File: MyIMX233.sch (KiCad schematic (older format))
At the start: 91 parts, among them IC1 iMX233, IC2 DDR_SDRAM_MT46_x16, J1 USB_OTG, P1 4p2, P2 1v2, P3 VDDA1v8, P4 2v5, P5 3v3, P6 1v, SW1 SWITCH_PUSHBUTTON, Y1 24Mhz

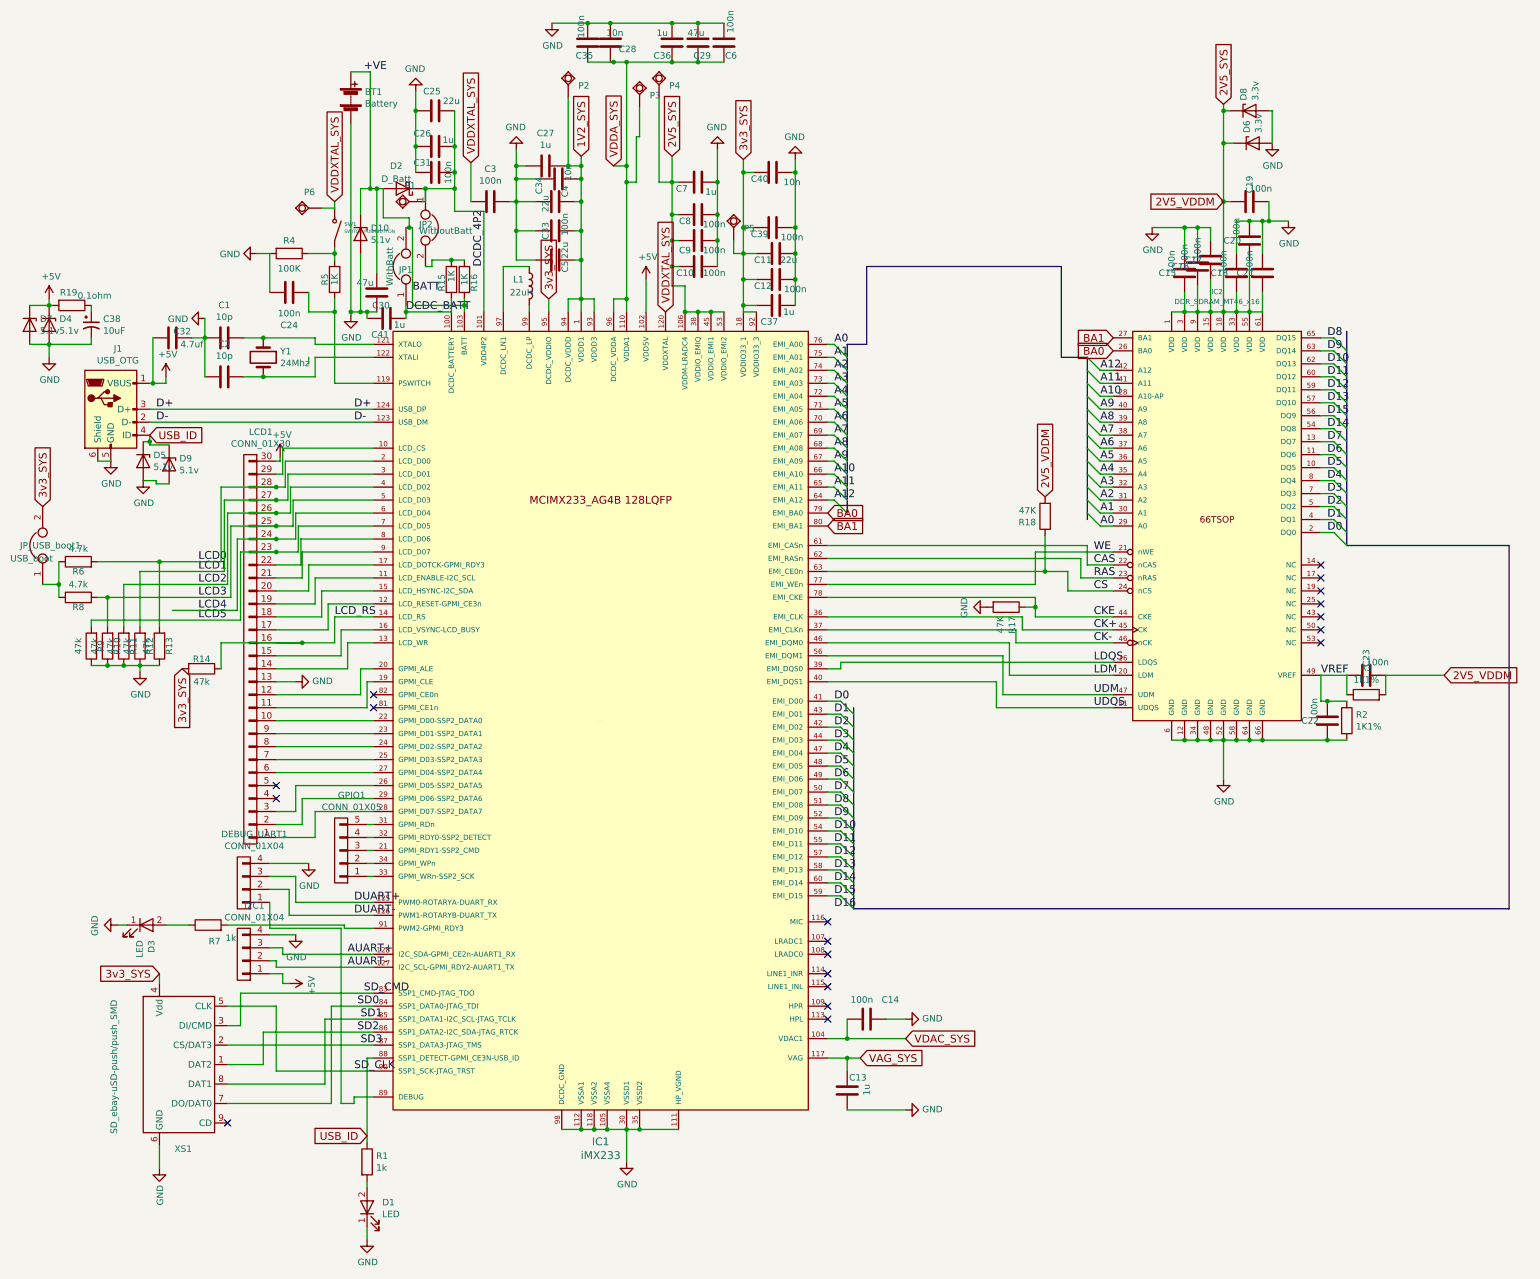
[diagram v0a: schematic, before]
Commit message: added  SD data resistors, clk nCLK resistor, series resistor to stop oscillation
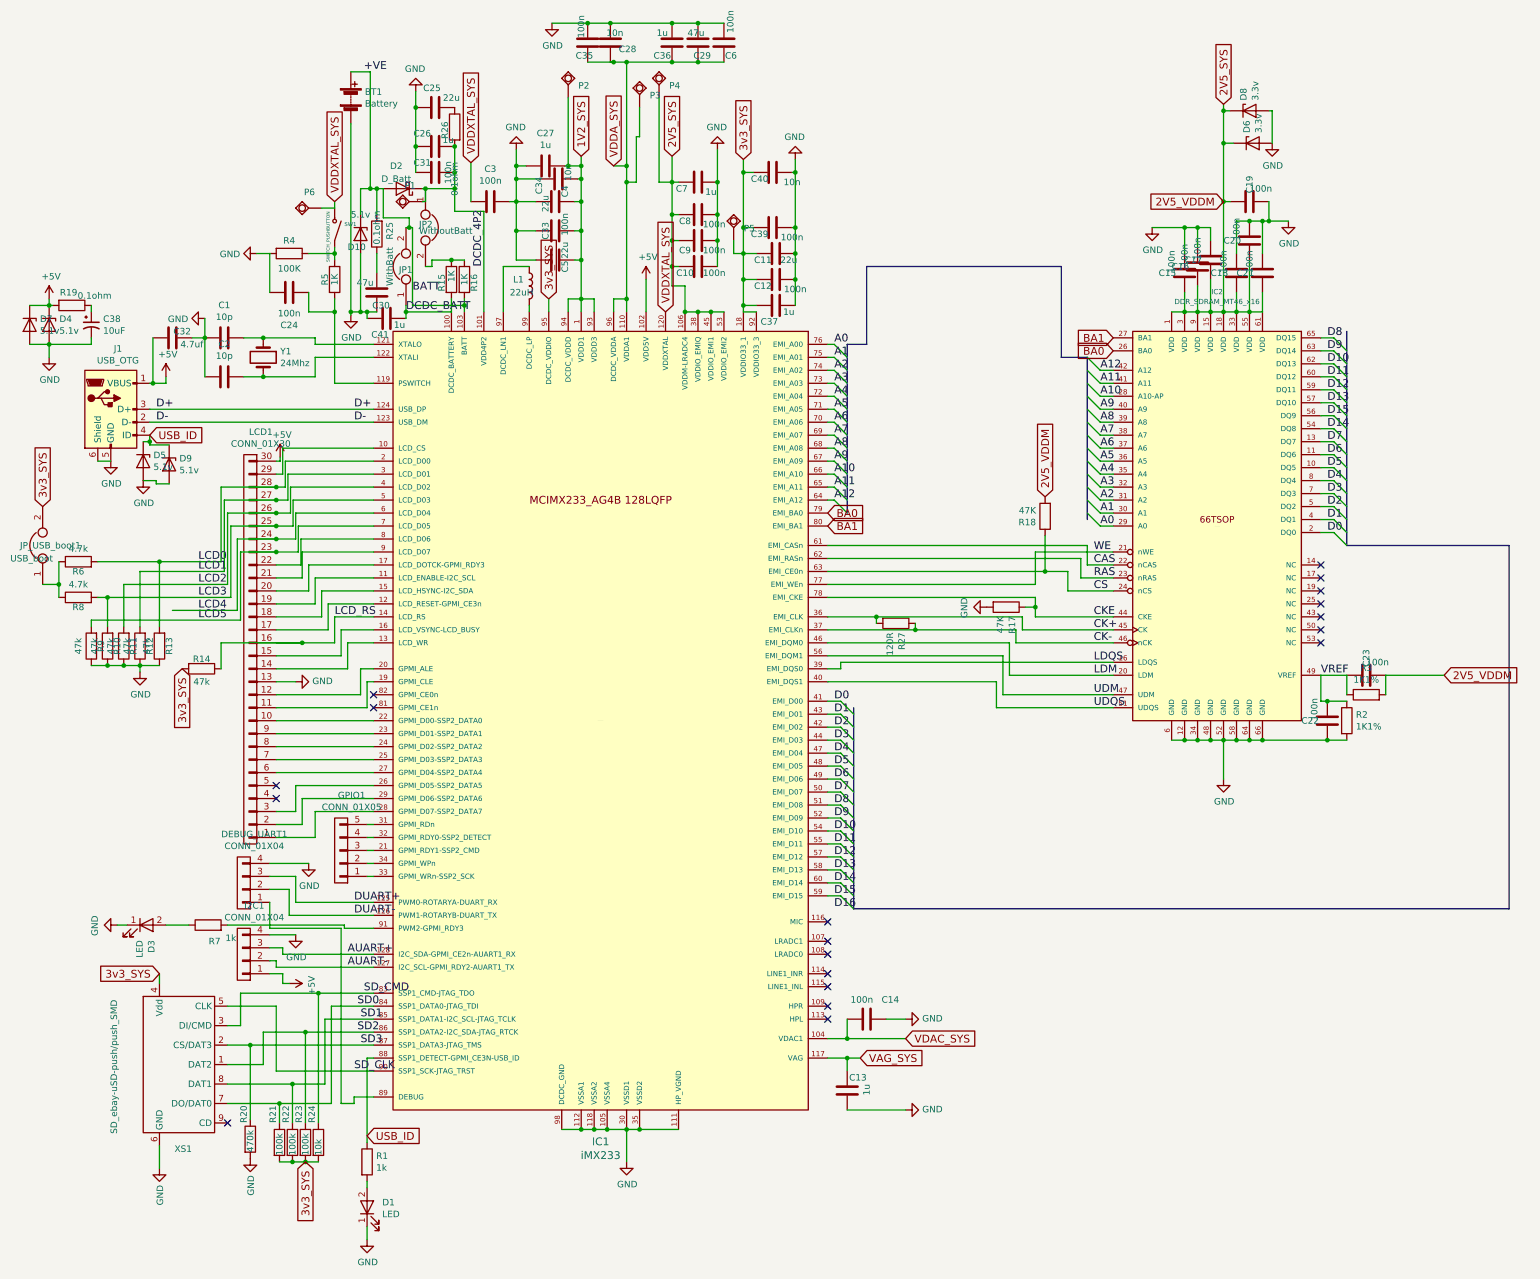
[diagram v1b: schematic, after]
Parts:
- added R20: 470k, Resistors_SMD:R_0603_HandSoldering, symbol R
- added R21, R22, R23: 100k, Resistors_SMD:R_0603_HandSoldering, symbol R
- added R24: 10k, Resistors_SMD:R_0603_HandSoldering, symbol R
- added R25, R26: 0.1ohm, Resistors_SMD:R_0603_HandSoldering, symbol R
- added R27: 120R, Resistors_SMD:R_0603, symbol R
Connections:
- net +VE: now also R25.2; no longer C30.1
- net 3v3_SYS: now also R21.2, R22.2, R23.2, R24.2
- net CK+: now also R27.2
- net CK-: now also R27.1
- net DCDC_4P2: now also R26.2; no longer C25.2
- net GND: now also R20.2
- net SD0: now also R21.1
- net SD1: now also R22.1
- net SD2: now also R23.1
- net SD3: now also R20.1
- net SD_CMD: now also R24.1
- new net: C25.2, R26.1
- new net: C30.1, R25.1
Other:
- moved on the sheet: C25
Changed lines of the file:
@@
 P 2950 2100
 F 0 "SW1" V 2924 2175 30  0000 L CNN
-F 1 "SWITCH_PUSHBUTTON" V 2980 2175 25  0000 L CNN
+F 1 "SWITCH_PUSHBUTTON" H 2825 2050 25  0000 L CNN
 F 2 "Buttons_Switches_THT:SW_PUSH_6mm" H 2950 2100 60  0001 C CNN
 F 3 "" H 2950 2100 60  0001 C CNN
@@
 L C C25
 U 1 1 592FCC84
-P 3725 1200
-F 0 "C25" V 3875 1225 50  0000 C CNN
-F 1 "22u" V 3800 1075 50  0000 C CNN
-F 2 "Capacitors_SMD:C_0805_HandSoldering" H 3763 1050 50  0001 C CNN
-F 3 "" H 3725 1200 50  0001 C CNN
-	1    3725 1200
+P 3725 1175
+F 0 "C25" V 3875 1200 50  0000 C CNN
+F 1 "22u" V 3800 1050 50  0000 C CNN
+F 2 "Capacitors_SMD:C_0805_HandSoldering" H 3763 1025 50  0001 C CNN
+F 3 "" H 3725 1175 50  0001 C CNN
+	1    3725 1175
 	0    -1   -1   0
 $EndComp
@@
 	1    0    0    -1
 $EndComp
-Text GLabel 3200 9100 0    60   Input ~ 0
+Text GLabel 3200 9100 2    60   Input ~ 0
 USB_ID
 Text GLabel 1525 3700 2    60   Input ~ 0
@@
 	2250 2950 2800 2950
 Connection ~ 2400 2950
-Wire Wire Line
-	2750 3100 2750 3150
 Wire Wire Line
 	1950 2800 1950 3250
@@
 Wire Wire Line
 	3575 1050 3575 1675
-Connection ~ 3575 1200
-Wire Wire Line
-	3875 1975 3875 1200
 Connection ~ 3875 1675
 Connection ~ 3875 1475
 Connection ~ 3575 1475
 Wire Wire Line
-	3625 1800 3875 1800
+	3875 1800 3625 1800
 Connection ~ 3875 1800
 Wire Wire Line
@@
 Connection ~ 3525 2100
 Wire Wire Line
-	3275 1800 3275 2450
-Wire Wire Line
 	3275 2750 3075 2750
 Connection ~ 3075 2750
@@
 U 1 1 59A40581
 P 3150 2150
-F 0 "D10" V 3104 2229 50  0000 L CNN
-F 1 "5.1v" V 3195 2229 50  0000 L CNN
+F 0 "D10" V 3250 2050 50  0000 L CNN
+F 1 "5.1v" V 3000 2075 50  0000 L CNN
 F 2 "Diodes_SMD:D_SOD-323_HandSoldering" H 3150 2150 50  0001 C CNN
 F 3 "" H 3150 2150 50  0001 C CNN
@@
 	3150 2300 3150 2750
 Connection ~ 3150 2750
+$Comp
+L R R26
+U 1 1 59A340AA
+P 3875 1325
+F 0 "R26" V 3950 1300 50  0000 C CNN
+F 1 "0.1ohm" V 3875 925 50  0000 C CNN
+F 2 "Resistors_SMD:R_0603_HandSoldering" V 3805 1325 50  0001 C CNN
+F 3 "" H 3875 1325 50  0001 C CNN
+	1    3875 1325
+	-1   0    0    -1
+$EndComp
+Connection ~ 3575 1175
+$Comp
+L R R25
+U 1 1 59A38C82
+P 3275 2150
+F 0 "R25" V 3175 2125 50  0000 C CNN
+F 1 "0.1ohm" V 3275 2100 50  0000 C CNN
+F 2 "Resistors_SMD:R_0603_HandSoldering" V 3205 2150 50  0001 C CNN
+F 3 "" H 3275 2150 50  0001 C CNN
+	1    3275 2150
+	-1   0    0    1
+$EndComp
+Wire Wire Line
+	3275 2300 3275 2450
+Wire Wire Line
+	3275 2000 3275 1800
+$Comp
+L R R20
+U 1 1 59A41AE4
+P 2300 9125
+F 0 "R20" V 2250 9250 50  0000 L CNN
+F 1 "470k" V 2300 9025 50  0000 L CNN
+F 2 "Resistors_SMD:R_0603_HandSoldering" V 2230 9125 50  0001 C CNN
+F 3 "" H 2300 9125 50  0001 C CNN
+	1    2300 9125
+	1    0    0    -1
+$EndComp
+$Comp
+L GND #PWR032
+U 1 1 59A429AF
+P 2300 9275
+F 0 "#PWR032" H 2300 9025 50  0001 C CNN
+F 1 "GND" V 2305 9147 50  0000 R CNN
+F 2 "" H 2300 9275 50  0001 C CNN
+F 3 "" H 2300 9275 50  0001 C CNN
+	1    2300 9275
+	1    0    0    -1
+$EndComp
+Wire Wire Line
+	2300 8975 2300 8400
+Connection ~ 2300 8400
+$Comp
+L R R27
+U 1 1 59A44B82
+P 7275 5150
+F 0 "R27" H 7345 5196 50  0000 L CNN
+F 1 "120R" H 7345 5105 50  0000 L CNN
+F 2 "Resistors_SMD:R_0603" V 7205 5150 50  0001 C CNN
+F 3 "" H 7275 5150 50  0001 C CNN
+	1    7275 5150
+	0    1    1    0
+$EndComp
+Wire Wire Line
+	7125 5150 7125 5100
+Connection ~ 7125 5100
+Wire Wire Line
+	7425 5150 7425 5200
+Connection ~ 7425 5200
+$Comp
+L R R21
+U 1 1 59A4733A
+P 2525 9150
+F 0 "R21" V 2475 9300 50  0000 L CNN
+F 1 "100k" V 2525 9050 50  0000 L CNN
+F 2 "Resistors_SMD:R_0603_HandSoldering" V 2455 9150 50  0001 C CNN
+F 3 "" H 2525 9150 50  0001 C CNN
+	1    2525 9150
+	1    0    0    -1
+$EndComp
+Wire Wire Line
+	2825 9000 2825 8000
+Connection ~ 2825 8000
+Wire Wire Line
+	2725 9000 2725 8300
+Connection ~ 2725 8300
+Wire Wire Line
+	2525 9300 2825 9300
+Connection ~ 2725 9300
+Connection ~ 2625 9300
+Text GLabel 2725 9300 3    60   Input ~ 0
+3v3_SYS
+$Comp
+L R R22
+U 1 1 59A4BB47
+P 2625 9150
+F 0 "R22" V 2575 9300 50  0000 L CNN
+F 1 "100k" V 2625 9050 50  0000 L CNN
+F 2 "Resistors_SMD:R_0603_HandSoldering" V 2555 9150 50  0001 C CNN
+F 3 "" H 2625 9150 50  0001 C CNN
+	1    2625 9150
+	1    0    0    -1
+$EndComp
+$Comp
+L R R23
+U 1 1 59A4BC29
+P 2725 9150
+F 0 "R23" V 2675 9300 50  0000 L CNN
+F 1 "100k" V 2725 9050 50  0000 L CNN
+F 2 "Resistors_SMD:R_0603_HandSoldering" V 2655 9150 50  0001 C CNN
+F 3 "" H 2725 9150 50  0001 C CNN
+	1    2725 9150
+	1    0    0    -1
+$EndComp
+$Comp
+L R R24
+U 1 1 59A4BD01
+P 2825 9150
+F 0 "R24" V 2775 9300 50  0000 L CNN
+F 1 "10k" V 2825 9050 50  0000 L CNN
+F 2 "Resistors_SMD:R_0603_HandSoldering" V 2755 9150 50  0001 C CNN
+F 3 "" H 2825 9150 50  0001 C CNN
+	1    2825 9150
+	1    0    0    -1
+$EndComp
+Wire Wire Line
+	3875 1975 3875 1475
+Wire Wire Line
+	2625 9000 2625 8700
+Connection ~ 2625 8700
+Wire Wire Line
+	2525 9000 2525 8850
+Connection ~ 2525 8850
 $EndSCHEMATC

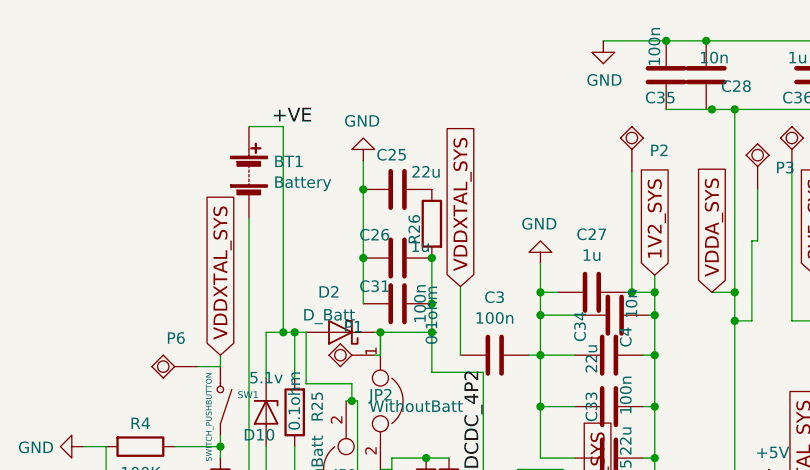
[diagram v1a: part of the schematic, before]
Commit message: added optional 22uf electrolyte cap in 4p2
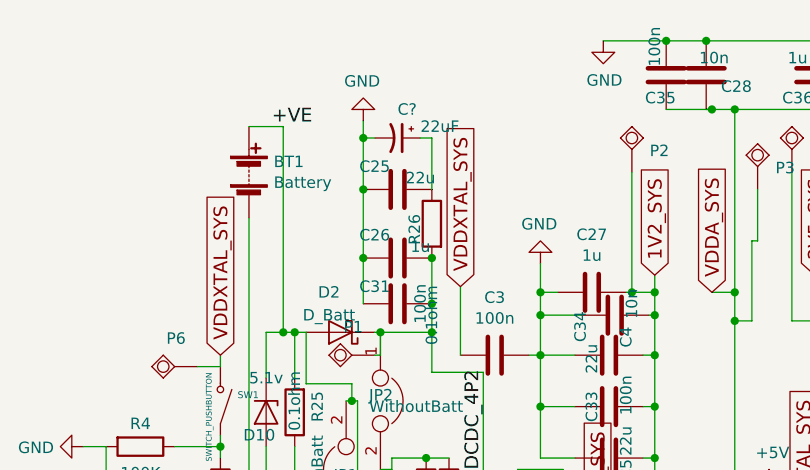
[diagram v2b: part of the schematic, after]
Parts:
- added C?: 22uF, Capacitors_THT:CP_Radial_D5.0mm_P2.50mm, symbol CP1_Small
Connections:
- net GND: now also C?.2
- net at C25.2, R26.1: now also C?.1
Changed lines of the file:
@@
 U 1 1 592FCC84
 P 3725 1175
-F 0 "C25" V 3875 1200 50  0000 C CNN
-F 1 "22u" V 3800 1050 50  0000 C CNN
+F 0 "C25" V 3825 1275 50  0000 C CNN
+F 1 "22u" V 3775 1075 50  0000 C CNN
 F 2 "Capacitors_SMD:C_0805_HandSoldering" H 3763 1025 50  0001 C CNN
 F 3 "" H 3725 1175 50  0001 C CNN
@@
 L GND #PWR022
 U 1 1 592FDAC8
-P 3575 1050
-F 0 "#PWR022" H 3575 800 50  0001 C CNN
-F 1 "GND" H 3580 877 50  0000 C CNN
-F 2 "" H 3575 1050 50  0001 C CNN
-F 3 "" H 3575 1050 50  0001 C CNN
-	1    3575 1050
+P 3575 875
+F 0 "#PWR022" H 3575 625 50  0001 C CNN
+F 1 "GND" H 3580 702 50  0000 C CNN
+F 2 "" H 3575 875 50  0001 C CNN
+F 3 "" H 3575 875 50  0001 C CNN
+	1    3575 875
 	-1   0    0    1
 $EndComp
@@
 	4100 1975 3875 1975
 Wire Wire Line
-	3575 1050 3575 1675
+	3575 875  3575 1675
 Connection ~ 3875 1675
 Connection ~ 3875 1475
@@
 	2525 9000 2525 8850
 Connection ~ 2525 8850
+$Comp
+L CP1_Small C?
+U 1 1 59A5D892
+P 3725 950
+F 0 "C?" V 3600 950 50  0000 L CNN
+F 1 "22uF" V 3675 1050 50  0000 L CNN
+F 2 "Capacitors_THT:CP_Radial_D5.0mm_P2.50mm" H 3725 950 50  0001 C CNN
+F 3 "" H 3725 950 50  0001 C CNN
+	1    3725 950
+	0    1    1    0
+$EndComp
+Wire Wire Line
+	3825 950  3875 950
+Wire Wire Line
+	3875 950  3875 1175
+Wire Wire Line
+	3625 950  3575 950
+Connection ~ 3575 950
 $EndSCHEMATC

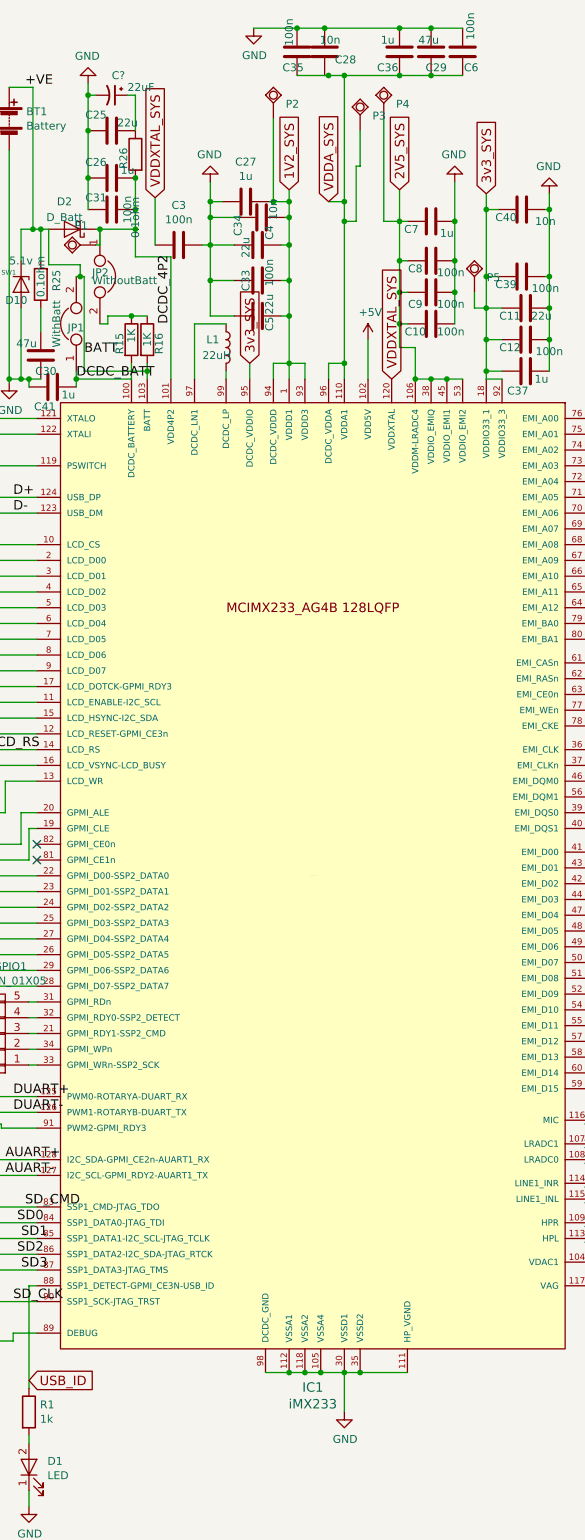
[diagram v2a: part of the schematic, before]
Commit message: mounting hole added once for all time in schematic
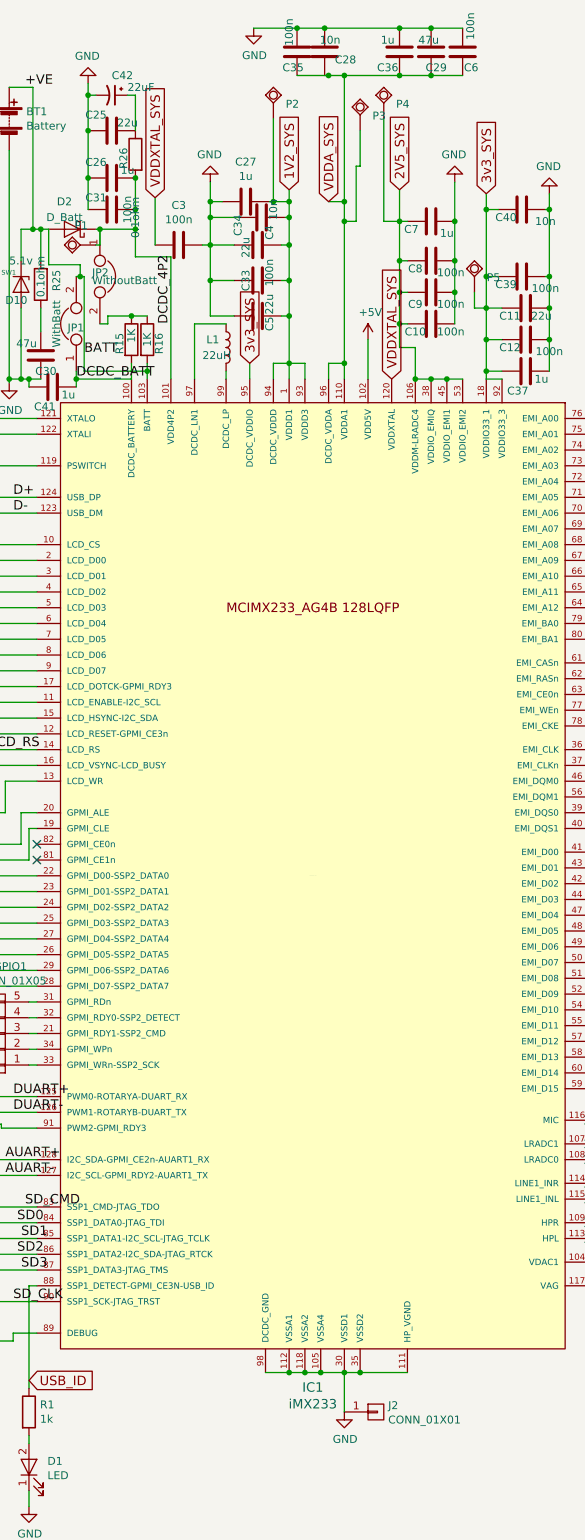
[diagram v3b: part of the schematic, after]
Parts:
- added J2: CONN_01X01, Connectors:1pin, symbol CONN_01X01
- gave numbers to parts that had none: 1
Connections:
- net GND: now also J2.1 (P1)
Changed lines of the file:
@@
 Connection ~ 2525 8850
 $Comp
-L CP1_Small C?
+L CP1_Small C42
 U 1 1 59A5D892
 P 3725 950
-F 0 "C?" V 3600 950 50  0000 L CNN
+F 0 "C42" V 3600 950 50  0000 L CNN
 F 1 "22uF" V 3675 1050 50  0000 L CNN
 F 2 "Capacitors_THT:CP_Radial_D5.0mm_P2.50mm" H 3725 950 50  0001 C CNN
@@
 	3625 950  3575 950
 Connection ~ 3575 950
+$Comp
+L CONN_01X01 J2
+U 1 1 59A6845B
+P 5400 9300
+F 0 "J2" H 5478 9341 50  0000 L CNN
+F 1 "CONN_01X01" H 5478 9250 50  0000 L CNN
+F 2 "Connectors:1pin" H 5400 9300 50  0001 C CNN
+F 3 "" H 5400 9300 50  0001 C CNN
+	1    5400 9300
+	1    0    0    -1
+$EndComp
 $EndSCHEMATC
